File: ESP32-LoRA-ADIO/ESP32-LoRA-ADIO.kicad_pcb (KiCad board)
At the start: 2 copper layers, 93 x 61 mm, 27 parts, among them J1 USB_B_Micro, J2 External Power, J3 AIO/I2C, J4 DIO, J5 RXTX+Power, J6 SMA, Q1 IRLML5203, Q2 2N7002, Q3 2N7002, U1 AP1117-33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

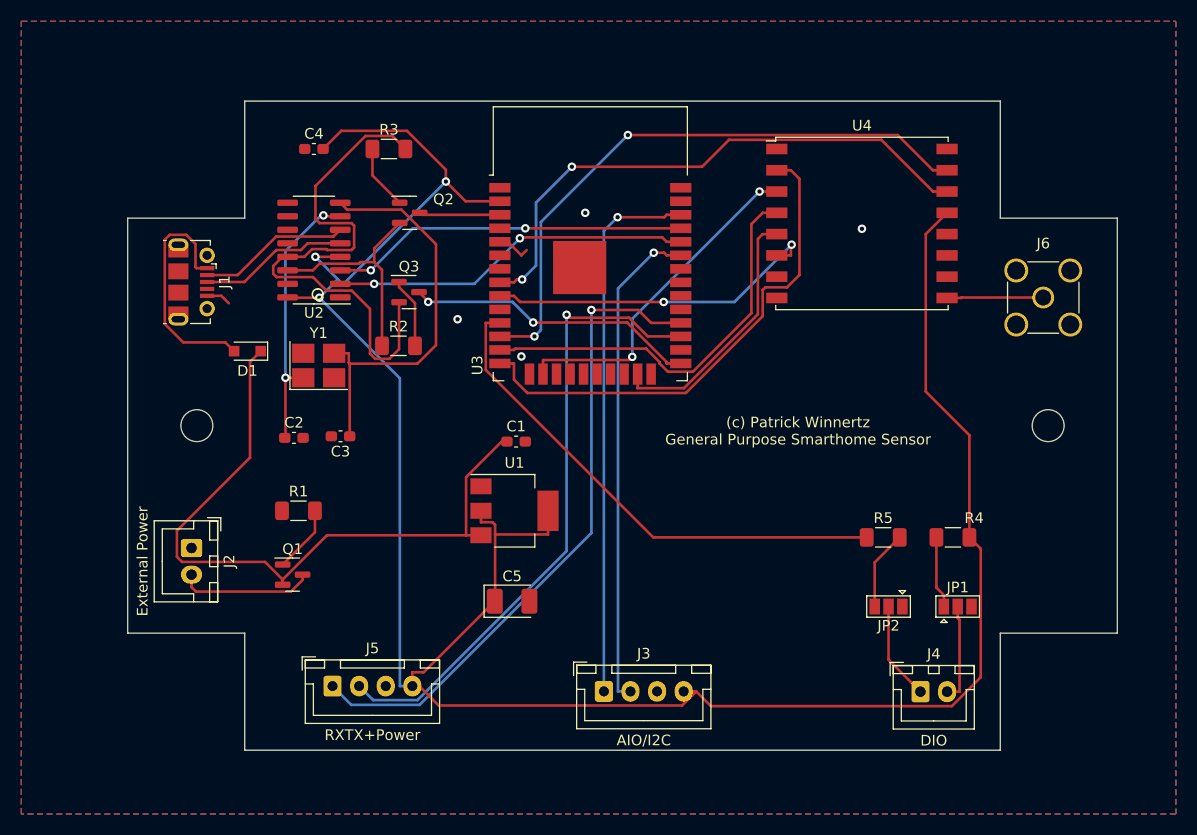
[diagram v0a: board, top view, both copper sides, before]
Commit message: Add a AI and add jumpers to the AI/I2C slot
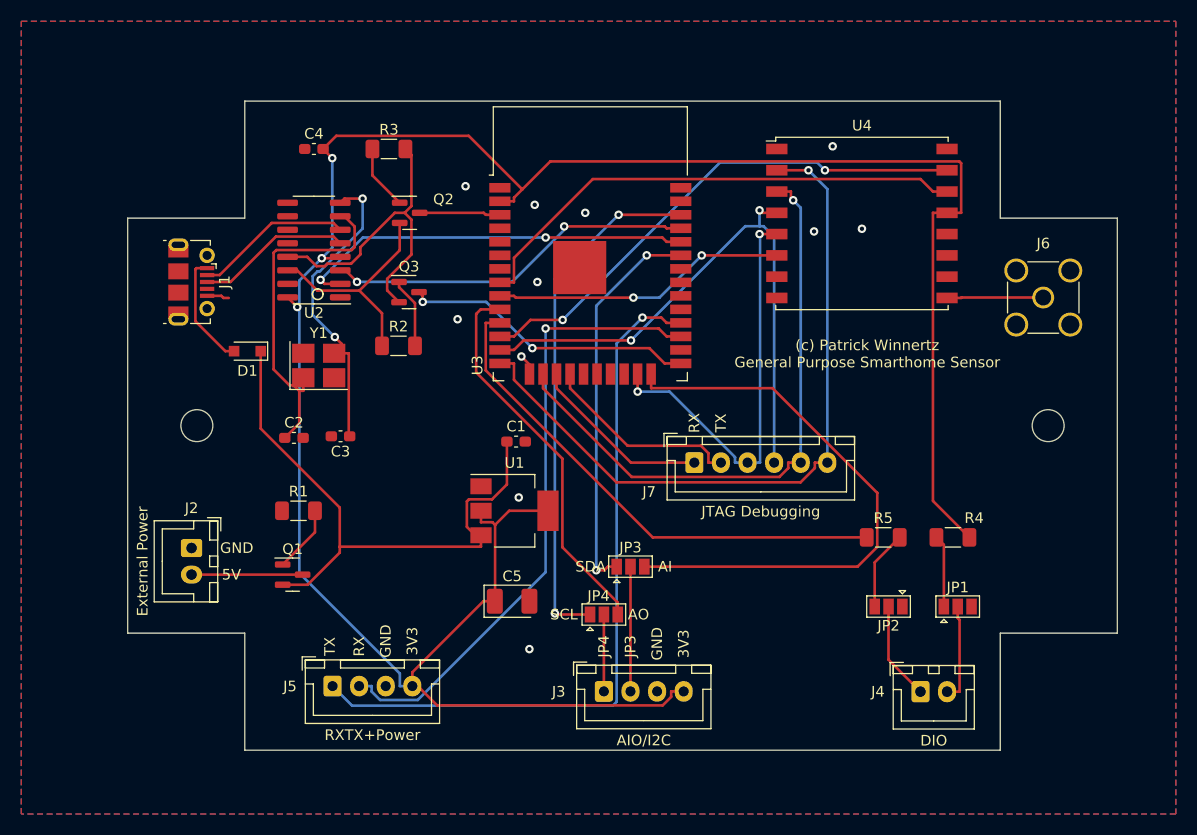
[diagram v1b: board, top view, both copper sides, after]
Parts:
- added J7: JTAG Debugging, Connector_JST:JST_XH_B6B-XH-A_1x06_P2.50mm_Vertical, F.Cu at (167.2, 60.0)
- added JP3: Jumper, Jumper:SolderJumper-3_P1.3mm_Open_Pad1.0x1.5mm, F.Cu at (161.2, 69.8)
- added JP4: Jumper, Jumper:SolderJumper-3_P1.3mm_Open_Pad1.0x1.5mm, F.Cu at (158.8, 74.2)
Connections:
- J3 pad 1: ESP-AO -> Net-(J3-Pad1)
- J3 pad 2: ESP-AI -> Net-(J3-Pad2)
- U3 pad 10: unconnected-(U3-Pad10) -> ESP-AO
- U3 pad 17: unconnected-(U3-Pad17) -> JTAG_RX
- U3 pad 18: unconnected-(U3-Pad18) -> JTAG_TX
- U3 pad 24: unconnected-(U3-Pad24) -> ESP-AI
- U3 pad 33: ESP-AI -> ESP-SDA
- U3 pad 36: ESP-AO -> ESP-SCL
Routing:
- net ESP-SCL: track 0.00 -> 49.1 mm, vias 0 -> 2
- net ESP-SDA: track 0.00 -> 36.8 mm, vias 0 -> 2
- net Lora_MOSI: track 31.9 -> 57.0 mm, vias 2 -> 1
- net Lora_MISO: track 47.7 -> 68.6 mm, vias 0 -> 1
- net DTR: track 51.0 -> 30.4 mm
- net JTAG_TX: track 0.00 -> 18.9 mm
- net Lora_SCK: track 38.1 -> 55.4 mm, vias 0 -> 2
- net JTAG_RX: track 0.00 -> 17.2 mm
- net ESP-AO: track 51.1 -> 36.2 mm, vias 1 -> 0
- net Lora_NSS: track 24.5 -> 39.3 mm, vias 0 -> 2
- net Net-(J3-Pad2): track 0.00 -> 11.7 mm
- net Net-(D1-Pad2): track 22.2 -> 10.8 mm
- net +5V: track 64.9 -> 55.7 mm
- net Net-(C3-Pad1): track 37.4 -> 29.2 mm, vias 0 -> 2
- net Lora_DIO1: track 57.2 -> 49.1 mm
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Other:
- board text added: "3V3"
- board text added: "5V"
- board text added: "AI"
- board text added: "AO"
- board text added: "GND"
- board text added: "JP3"
- board text added: "JP4"
- board text added: "RX"
- board text added: "SCL"
- board text added: "SDA"
- board text added: "TX"

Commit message: Autorouting the new spi wiring
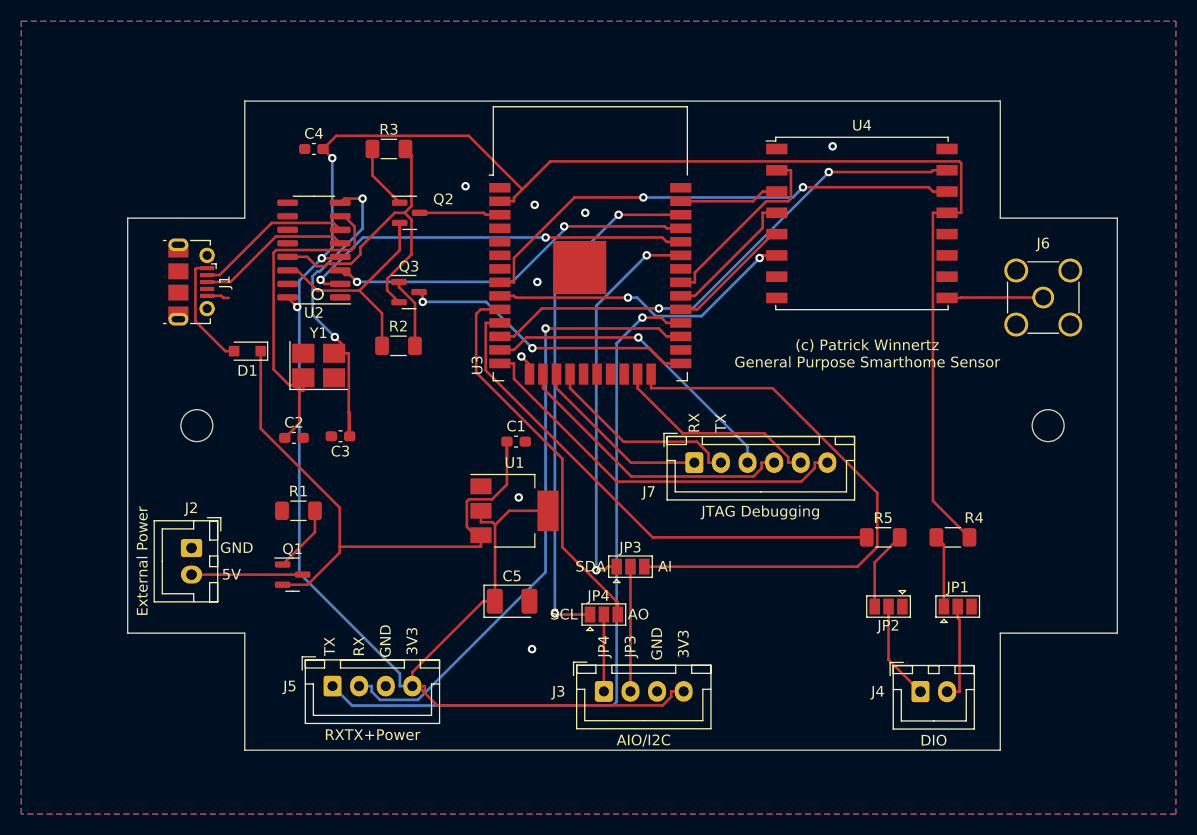
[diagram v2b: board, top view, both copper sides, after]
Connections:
- J7 pad 3: Lora_NSS -> JTAG_TMS
- J7 pad 4: Lora_SCK -> JTAG_TCK
- J7 pad 5: Lora_MOSI -> JTAG_TDO
- J7 pad 6: Lora_MISO -> JTAG_TDI
- U3 pad 13: Lora_SCK -> JTAG_TMS
- U3 pad 14: Lora_MISO -> JTAG_TDI
- U3 pad 16: Lora_MOSI -> JTAG_TCK
- U3 pad 23: Lora_NSS -> JTAG_TDO
- U3 pad 29: unconnected-(U3-Pad29) -> Lora_NSS
- U3 pad 30: unconnected-(U3-Pad30) -> Lora_SCK
- U3 pad 31: unconnected-(U3-Pad31) -> Lora_MISO
- U3 pad 37: unconnected-(U3-Pad37) -> Lora_MOSI
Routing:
- net Lora_MISO: track 68.6 -> 18.1 mm, vias 1 -> 0
- net Lora_MOSI: track 57.0 -> 9.40 mm, vias 1 -> 0
- net Lora_SCK: track 55.4 -> 13.1 mm, vias 2 -> 0
- net JTAG_TDI: track 0.00 -> 37.3 mm
- net JTAG_TMS: track 0.00 -> 29.5 mm, vias 0 -> 1
- net Lora_NSS: track 39.3 -> 12.0 mm, vias 2 -> 0
- net JTAG_TCK: track 0.00 -> 27.3 mm
- net JTAG_TDO: track 0.00 -> 19.9 mm
- net Net-(C3-Pad1): track 29.2 -> 31.4 mm
- net +5V: track 55.7 -> 57.2 mm
- net Lora_RST: track 27.7 -> 29.2 mm
- net +3V3: track 220.5 -> 221.9 mm
- net RTS: track 21.5 -> 22.8 mm
- net Lora_DIO0: track 47.9 -> 47.2 mm, vias 0 -> 2
- net UART-RX: track 34.9 -> 35.5 mm
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
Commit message: Added labels and get rid of some warnings
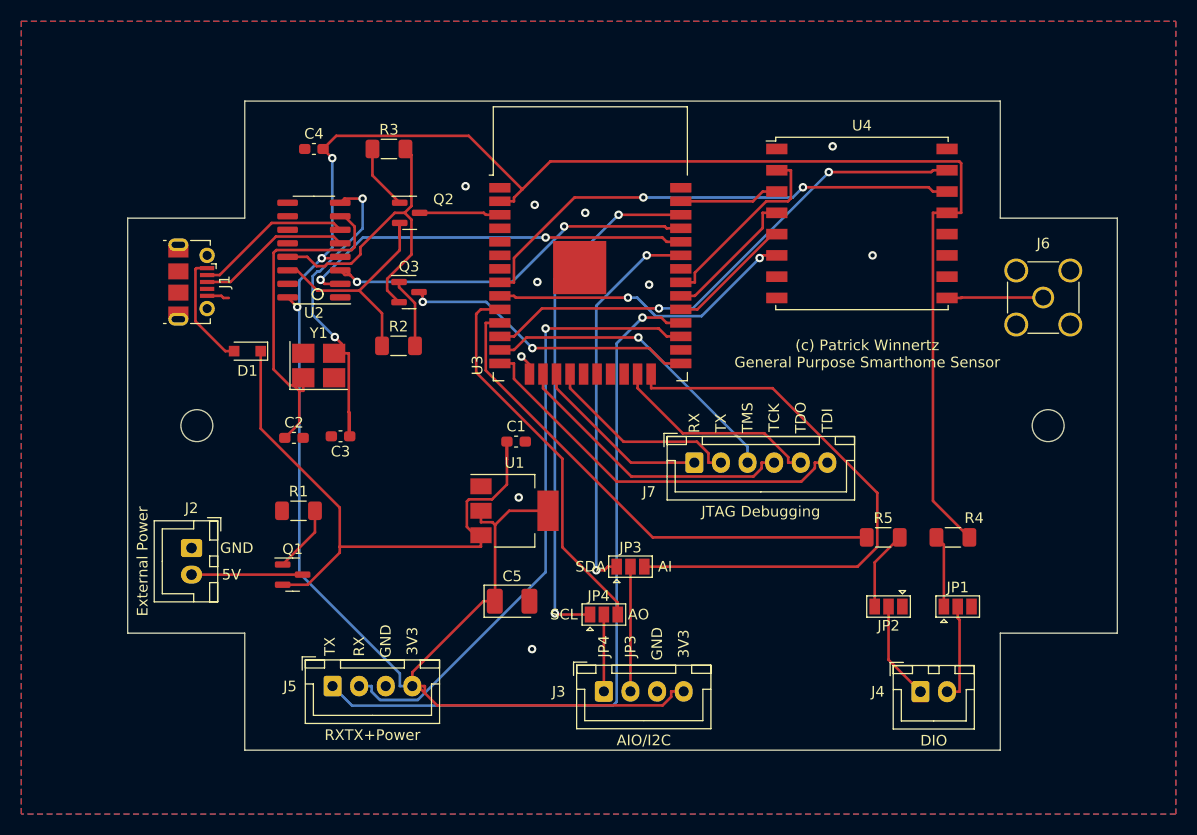
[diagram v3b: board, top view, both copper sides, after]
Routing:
- net +5V: track 57.2 -> 56.4 mm
- net Net-(C3-Pad1): track 31.4 -> 30.7 mm
- net Earth: vias 8 -> 10
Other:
- board text added: "TCK"
- board text added: "TDI"
- board text added: "TDO"
- board text added: "TMS"

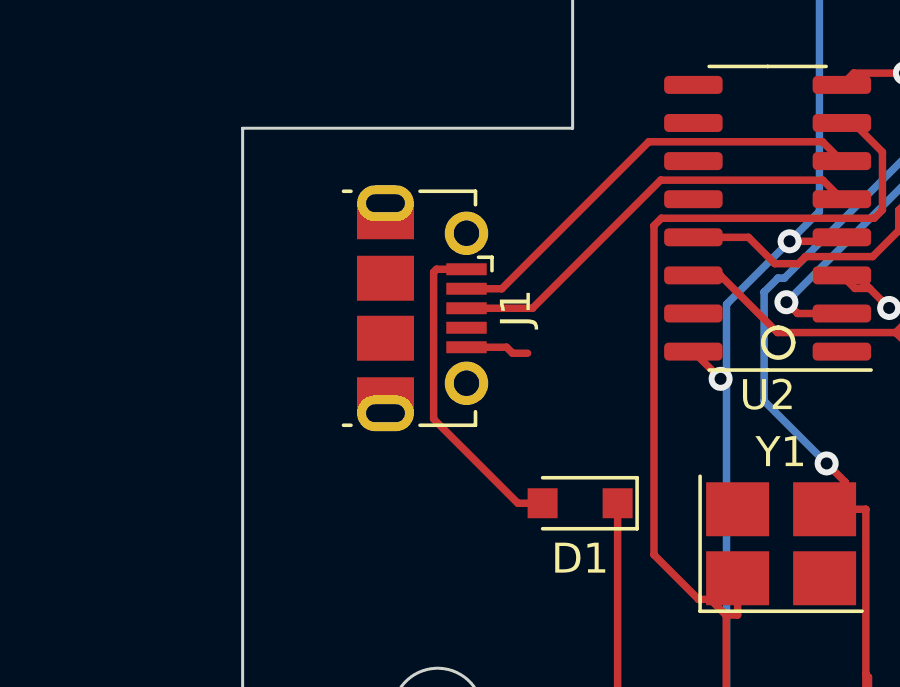
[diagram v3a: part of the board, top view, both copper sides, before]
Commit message: Replaced the Micro USB connector by a vertical one
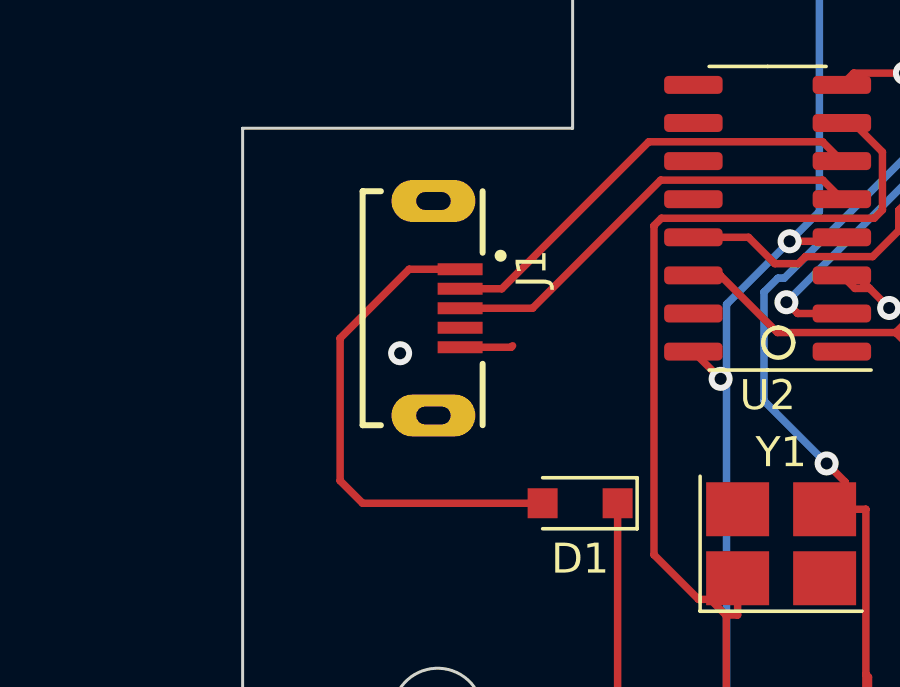
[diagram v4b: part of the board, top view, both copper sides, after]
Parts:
- J1: footprint Connector_USB:USB_Micro-B_Molex-105017-0001 -> USB3140-30-0230-1-C_REVE1:GCT_USB3140-30-0230-1-C_REVE1
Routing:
- net Net-(D1-Pad2): track 10.8 -> 16.8 mm
- net Earth: track 4.09 -> 3.74 mm, vias 10 -> 11
